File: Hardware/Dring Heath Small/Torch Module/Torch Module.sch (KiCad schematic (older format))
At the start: 53 parts, among them J1 Torch, J10 Module conn, J11 Conn_01x18_Male, J2 Module3, J3 Conn_01x18_Male, J4 Limit, J6 Motor, J7 Module1, J8 Torch, J9 2.54 pin, K1 G6E, Q1 IRLML2402, Q2 IRLML2402, Q3 IRLML2402, Q4 IRLML2402, Q5 IRLML2402, U1 ULN2002

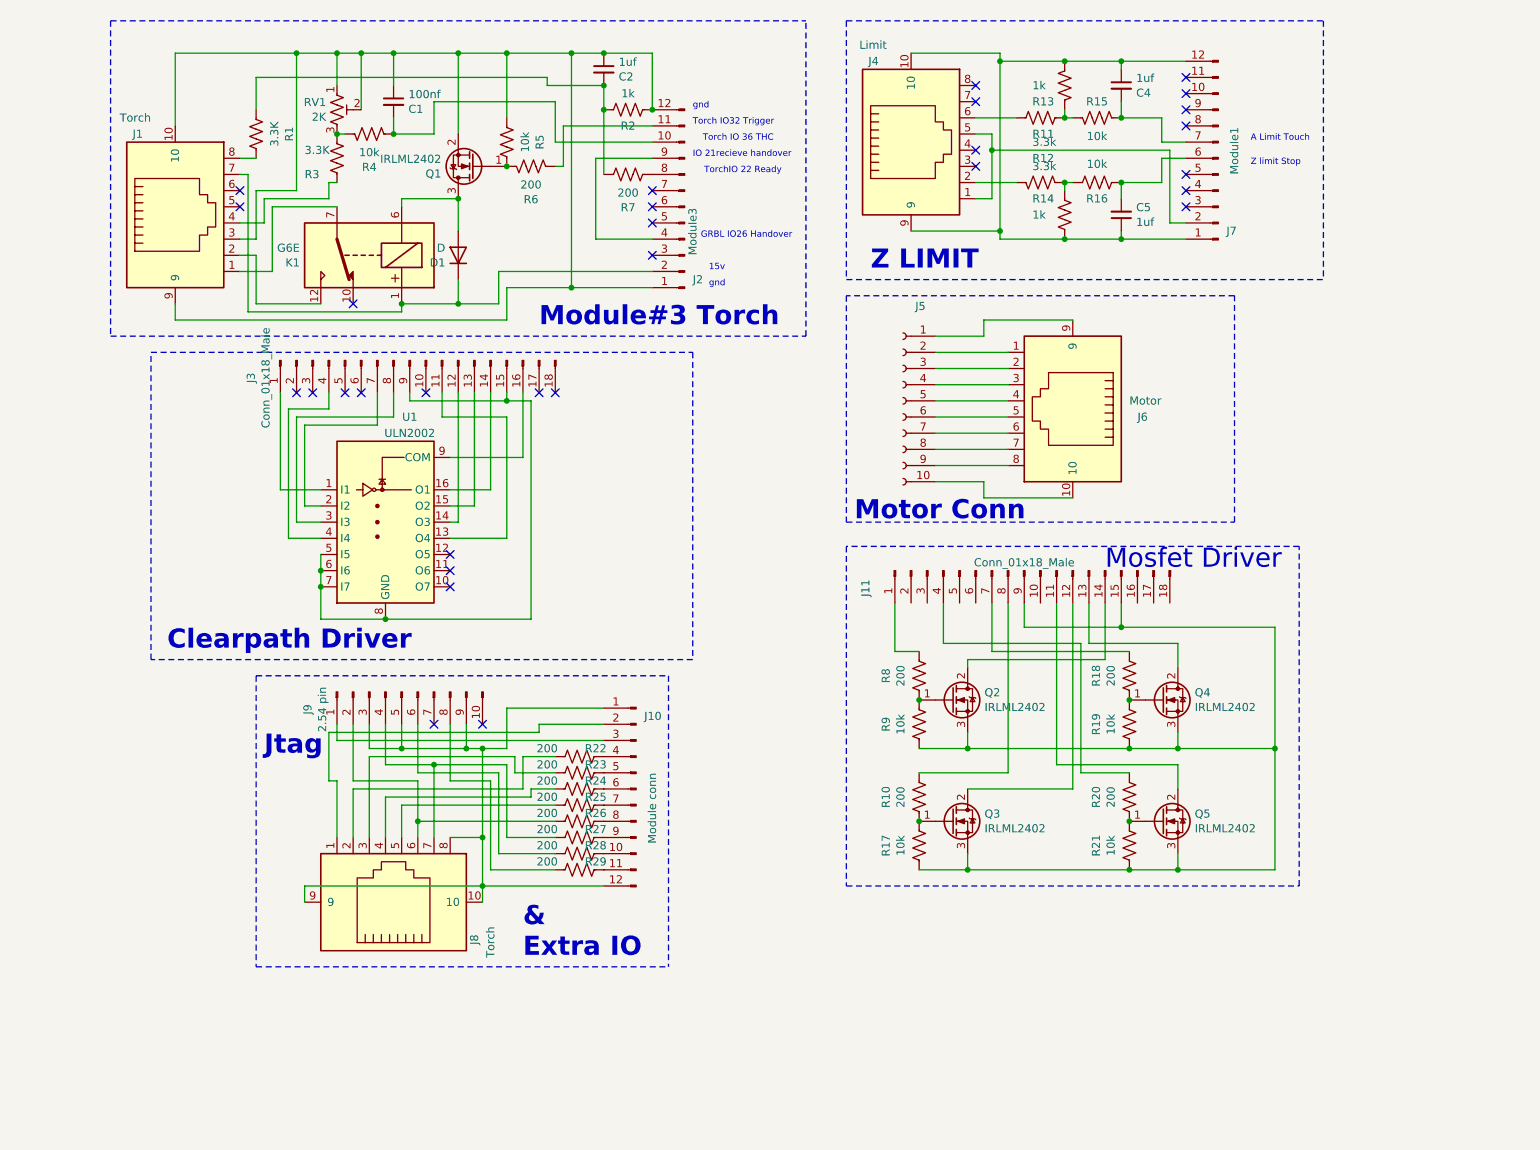
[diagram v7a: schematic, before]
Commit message: Added external A/D ADS1115
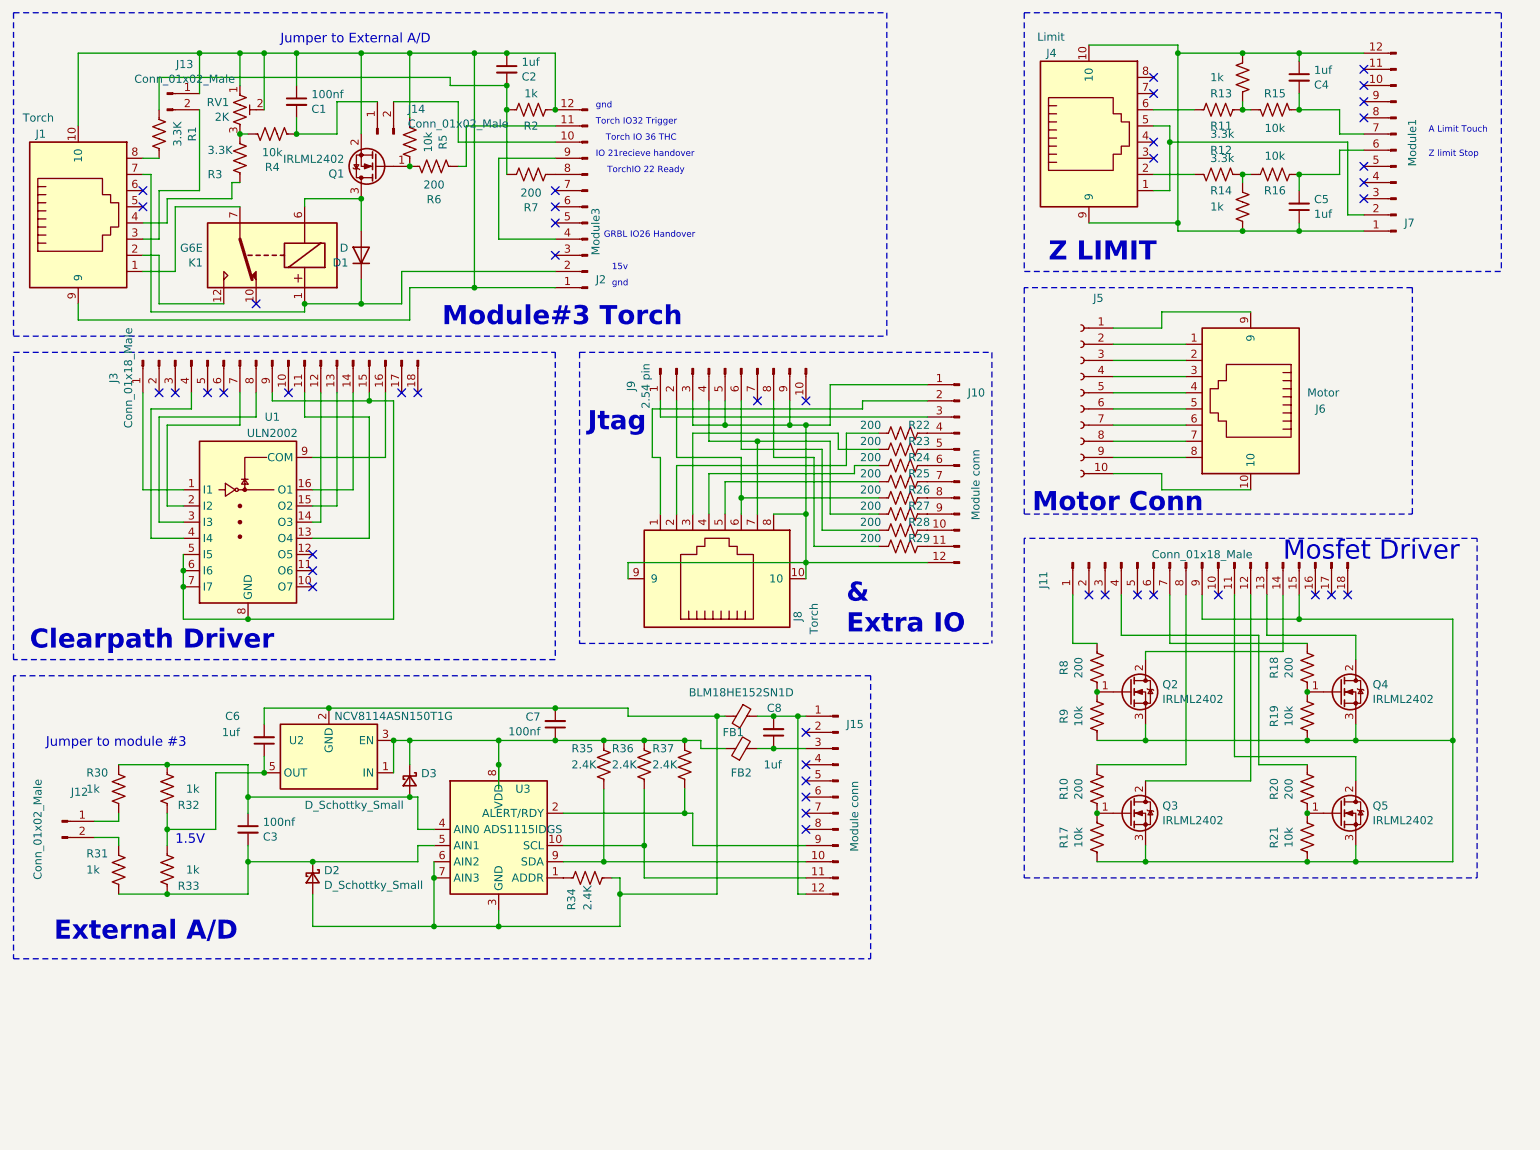
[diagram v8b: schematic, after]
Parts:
- added C3, C7: 100nf, Capacitor_SMD:C_0603_1608Metric_Pad1.08x0.95mm_HandSolder, symbol Device:C_Small
- added C6, C8: 1uf, Capacitor_SMD:C_0603_1608Metric_Pad1.08x0.95mm_HandSolder, symbol Device:C_Small
- added D2, D3: D_Schottky_Small, Diode_SMD:D_0805_2012Metric_Pad1.15x1.40mm_HandSolder, symbol Device:D_Schottky_Small
- added FB1: BLM18HE152SN1D, Resistor_SMD:R_0603_1608Metric_Pad0.98x0.95mm_HandSolder, symbol Device:Ferrite_Bead_Small
- added FB2: ~, Resistor_SMD:R_0603_1608Metric_Pad0.98x0.95mm_HandSolder, symbol Device:Ferrite_Bead_Small
- added J12, J13, J14: Conn_01x02_Male, Connector_PinHeader_2.54mm:PinHeader_1x02_P2.54mm_Vertical, symbol Connector:Conn_01x02_Male
- added J15: Module conn, Connector_PinHeader_2.54mm:PinHeader_1x12_P2.54mm_Vertical, symbol Connector:Conn_01x12_Male
- added R30, R31, R32, R33: 1k, Resistor_SMD:R_0603_1608Metric_Pad0.98x0.95mm_HandSolder, symbol Device:R_US
- added R34, R35, R36, R37: 2.4K, Resistor_SMD:R_0603_1608Metric_Pad0.98x0.95mm_HandSolder, symbol Device:R_US
- added U2: NCV8114ASN150T1G, Package_TO_SOT_SMD:TSOT-23-5, symbol Regulator_Linear:NCV8114ASN150T1G
- added U3: ADS1115IDGS, Package_SO:TSSOP-10_3x3mm_P0.5mm, symbol Analog_ADC:ADS1115IDGS
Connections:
- net at C1.1, C2.1, J1.10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: now also J13.1 (Pin_1); no longer J1.3
- net at C1.2, R4.1: now also J14.1 (Pin_1); no longer J2.10 (Pin_10)
- new net: J1.3, J13.2 (Pin_2)
- new net: R34.1, U3.1 (ADDR)
- new net: J15.11 (Pin_11), R36.2, U3.10 (SCL)
- new net: J15.9 (Pin_9), R37.2, U3.2 (ALERT/RDY)
- new net: C6.2, C7.2, D2.2 (A), FB1.2, R34.2, U2.2 (GND), U3.3 (GND), U3.6 (AIN2), U3.7 (AIN3)
- new net: C3.1, D3.2 (A), R30.1, R32.2, U3.4 (AIN0)
- new net: C3.2, D2.1 (K), R31.2, R33.1, U3.5 (AIN1)
- new net: C7.1, D3.1 (K), FB2.1, R35.1, R36.1, R37.1, U2.1 (IN), U2.3 (EN), U3.8 (VDD)
- new net: J15.10 (Pin_10), R35.2, U3.9 (SDA)
- new net: C8.2, FB1.1, J15.1 (Pin_1), J15.12 (Pin_12)
- new net: C8.1, FB2.2, J15.3 (Pin_3)
- new net: J14.2 (Pin_2), J2.10 (Pin_10)
- new net: J12.1 (Pin_1), R30.2
- new net: J12.2 (Pin_2), R31.1
- new net: C6.1, R32.1, R33.2, U2.5 (OUT)
- no-connect marks 30 -> 44
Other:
- note added: "1.5V"
- note added: "External A/D"
- note added: "Jumper to External A/D\n"
- note added: "Jumper to module #3\n"
- moved on the sheet: C1, C2, C4, C5, D1, J1, J10, J11, J2, J3, J4, J5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
